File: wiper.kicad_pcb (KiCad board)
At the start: 2 copper layers, 90 x 67.5 mm, 68 parts, among them J1 Conn_01x02, J10 Conn_01x02, J2 Sensor FW, J3 Sensor BK, J4 Conn_01x02, J5 Conn_01x02, J6 PROG, J7 I2C, J8 UART, J9 Conn_01x02, K1 G5LE-1, K2 G5LE-1, Q1 MMBT2222A, Q2 MMBT2222A, Q3 MMBT2222A, Q4 MMBT2222A, SW1 Reset, U1 LM7805_TO220, U2 PC817, U3 PC817, U4 KA78M05_TO252, U5 ATmega48-20A, Y1 16MHz

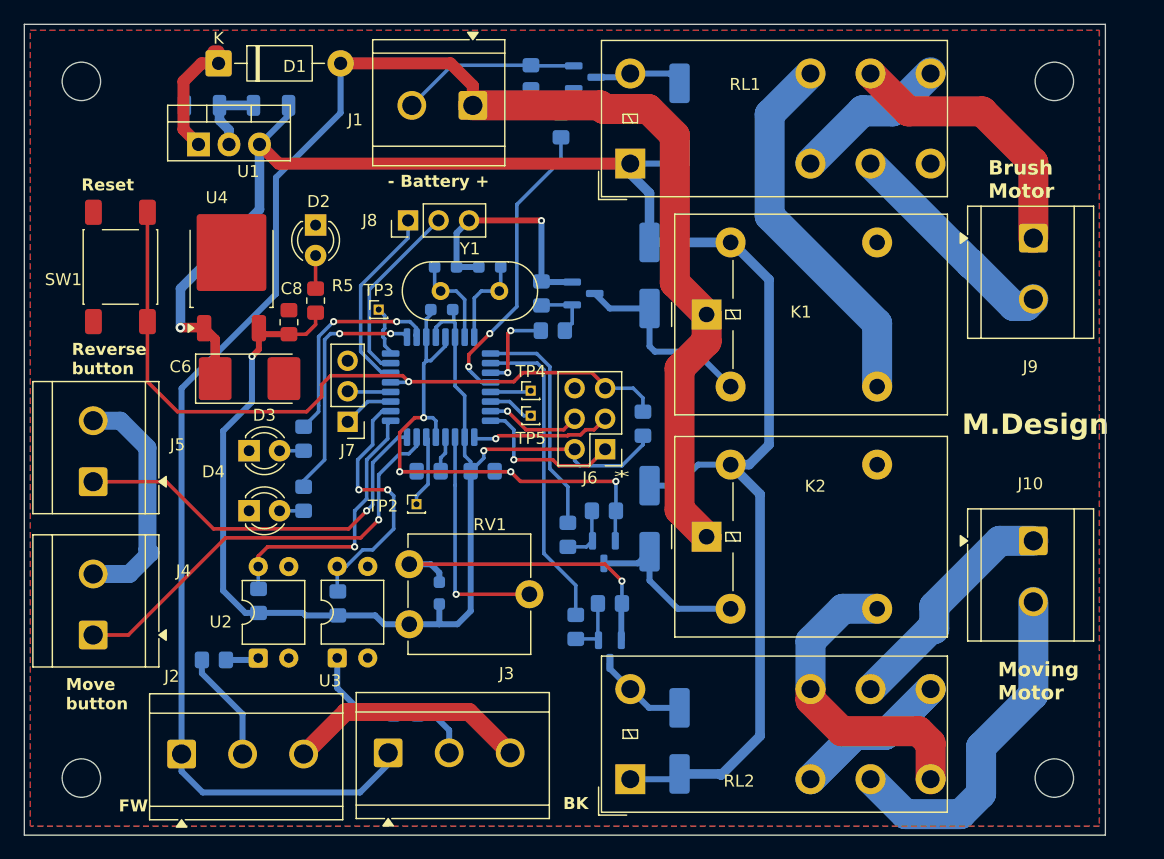
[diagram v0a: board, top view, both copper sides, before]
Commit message: New tracing finished. No mounting holes.
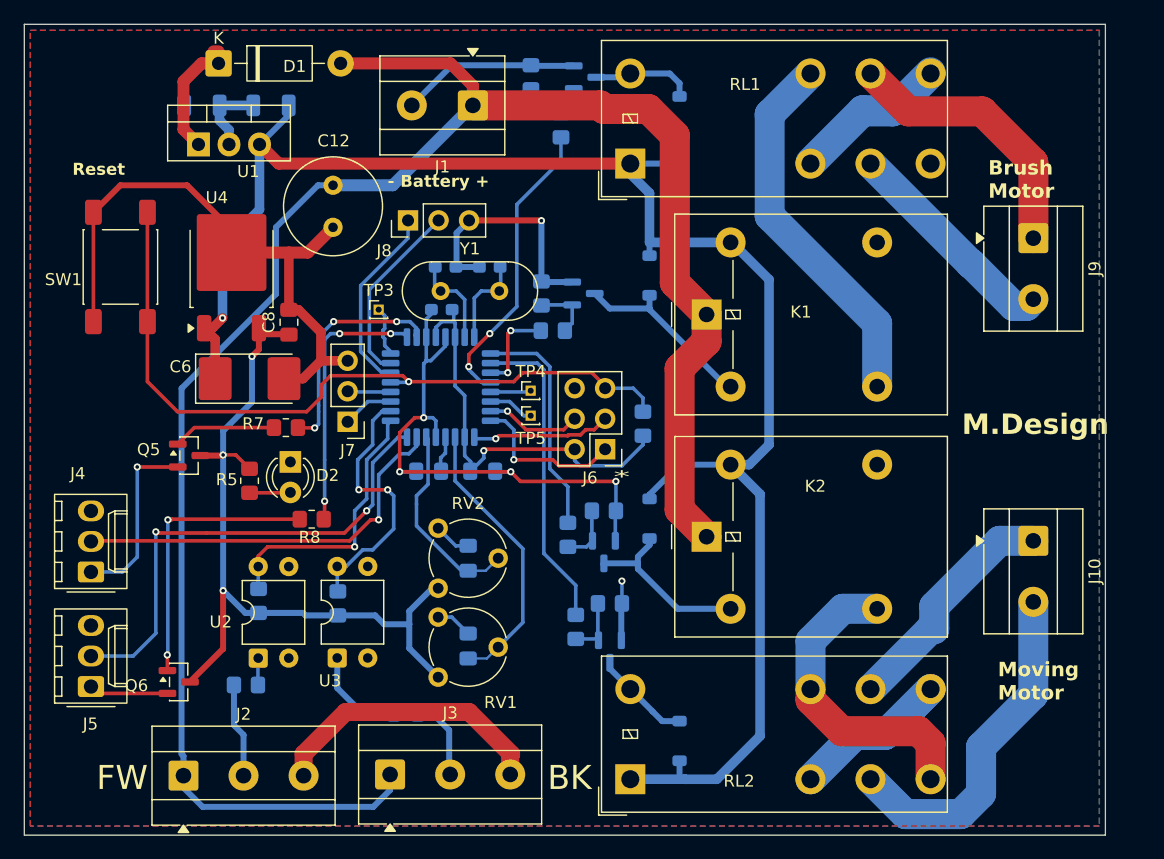
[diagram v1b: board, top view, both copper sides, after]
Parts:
- removed D3: LED MOVING, LED_THT:LED_D3.0mm
- removed D4: LED REVERSE, LED_THT:LED_D3.0mm
- removed REF** (x4): MountingHole_3.2mm_M3, MountingHole:MountingHole_3.2mm_M3
- removed TP2: ~, Connector_PinHeader_1.00mm:PinHeader_1x01_P1.00mm_Vertical
- added C11: 100nF, Capacitor_SMD:C_0805_2012Metric_Pad1.18x1.45mm_HandSolder, B.Cu at (175.2, 94.7)
- added C12: 47uFx100V, Capacitor_THT:C_Radial_D8.0mm_H7.0mm_P3.50mm, F.Cu at (163.9, 63.6)
- added Q5: MMBT2222A, Package_TO_SOT_SMD:SOT-23, F.Cu at (152.0, 86.2)
- added Q6: MMBT2222A, Package_TO_SOT_SMD:SOT-23, F.Cu at (151.1, 105.0)
- added RV2: 10K, Potentiometer_THT:Potentiometer_Piher_PT-6-V_Vertical, F.Cu at (172.7, 97.2)
- C1, C2: footprint Resistor_SMD:R_1206_3216Metric -> Capacitor_SMD:C_1206_3216Metric
- C10: footprint Resistor_SMD:R_0603_1608Metric_Pad0.98x0.95mm_HandSolder -> Capacitor_SMD:C_0805_2012Metric_Pad1.18x1.45mm_HandSolder
- C3, C4, C9: footprint Resistor_SMD:R_0603_1608Metric_Pad0.98x0.95mm_HandSolder -> Capacitor_SMD:C_0603_1608Metric_Pad1.08x0.95mm_HandSolder
- C5, C8: footprint Resistor_SMD:R_0805_2012Metric_Pad1.20x1.40mm_HandSolder -> Capacitor_SMD:C_0805_2012Metric_Pad1.18x1.45mm_HandSolder
- C7: value 100nF -> 10uF; footprint Resistor_SMD:R_0805_2012Metric_Pad1.20x1.40mm_HandSolder -> Capacitor_SMD:C_0805_2012Metric_Pad1.18x1.45mm_HandSolder
- D5, D6, D7, D8: value 1N4148 -> 1N4148W; footprint Diode_SMD:D_MiniMELF_Handsoldering -> Diode_SMD:D_SOD-123
- J1: value Conn_01x02 -> PWR_IN; footprint TerminalBlock_CUI:TerminalBlock_CUI_TB007-508-02_1x02_P5.08mm_Horizontal -> TerminalBlock_MetzConnect:TerminalBlock_MetzConnect_Type101_RT01602HBWC_1x02_P5.08mm_Horizontal
- J10: value Conn_01x02 -> MOTOR_MOVING; footprint TerminalBlock_CUI:TerminalBlock_CUI_TB007-508-02_1x02_P5.08mm_Horizontal -> TerminalBlock_MetzConnect:TerminalBlock_MetzConnect_Type101_RT01602HBWC_1x02_P5.08mm_Horizontal
- J2, J3: footprint TerminalBlock_CUI:TerminalBlock_CUI_TB007-508-03_1x03_P5.08mm_Horizontal -> TerminalBlock_MetzConnect:TerminalBlock_MetzConnect_Type055_RT01503HDWU_1x03_P5.00mm_Horizontal
- J4: value Conn_01x02 -> MOVE_BTN; footprint TerminalBlock_CUI:TerminalBlock_CUI_TB007-508-02_1x02_P5.08mm_Horizontal -> Connector_Molex:Molex_KK-254_AE-6410-03A_1x03_P2.54mm_Vertical
- J5: value Conn_01x02 -> REV_BTN; footprint TerminalBlock_CUI:TerminalBlock_CUI_TB007-508-02_1x02_P5.08mm_Horizontal -> Connector_Molex:Molex_KK-254_AE-6410-03A_1x03_P2.54mm_Vertical
- J9: value Conn_01x02 -> MOTOR_BRUSH; footprint TerminalBlock_CUI:TerminalBlock_CUI_TB007-508-02_1x02_P5.08mm_Horizontal -> TerminalBlock_MetzConnect:TerminalBlock_MetzConnect_Type101_RT01602HBWC_1x02_P5.08mm_Horizontal
- R7, R8: moved to F.Cu
- RV1: footprint Potentiometer_THT:Potentiometer_ACP_CA9-V10_Vertical -> Potentiometer_THT:Potentiometer_Piher_PT-6-V_Vertical
- U1: value LM7805_TO220 -> LM7812_TO220
- moved D2 19.8 mm to (160.4, 86.7)
- moved J5 17.1 mm to (143.8, 105.4)
- moved R5 16.0 mm to (157.0, 88.2), turned to -90 degrees
- moved J4 5.25 mm to (143.8, 95.8)
- moved C10 5.02 mm to (175.2, 102.0)
- moved RV1 5.02 mm to (172.7, 104.6)
- moved R1 3.39 mm to (156.7, 105.2)
- moved R8 1.83 mm to (162.2, 91.5), turned to 180 degrees
- moved J2 1.81 mm to (151.5, 112.8)
- moved J3 1.81 mm to (168.7, 112.7)
- moved R7 1.74 mm to (160.0, 83.8), turned to 180 degrees
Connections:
- C1 pad 2: Net-(U1-GND) -> ~
- C10 pad 1: +5V -> Net-(U5-ADC6)
- C2 pad 2: Net-(U1-GND) -> ~
- J4 pad 1: /MOVE_BTN -> Net-(J4-Pin_1)
- J4 pad 2: ~ -> /MOVE_BTN
- J5 pad 1: /REV_BTN -> Net-(J5-Pin_1)
- J5 pad 2: ~ -> /REV_BTN
- U1 pad 2: Net-(U1-GND) -> ~
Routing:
- net ~: track 200.3 -> 225.9 mm
- net Net-(Q6-B): track 2.00 -> 23.6 mm, vias 0 -> 2
- net Net-(J4-Pin_1): track 0.00 -> 15.2 mm, vias 0 -> 1
- net Net-(U5-ADC7): track 6.04 -> 16.6 mm
- net /REV_BTN: track 33.0 -> 40.9 mm, vias 1 -> 2
- net Net-(J5-Pin_1): track 0.00 -> 6.60 mm
- net Net-(Q5-B): track 2.00 -> 8.57 mm
- net Net-(U1-GND): track 6.40 -> 0.00 mm
- net +24V: track 206.1 -> 212.2 mm
- net Net-(U5-ADC6): track 19.2 -> 23.6 mm, vias 1 -> 0
- net /MOVE_BTN: track 36.4 -> 33.3 mm
- net +12V: track 144.7 -> 146.8 mm
- net Net-(U5-PD3): track 20.2 -> 22.2 mm, vias 2 -> 3
- net Net-(J3-Pin_2): track 5.09 -> 6.92 mm
- net Net-(J2-Pin_2): track 9.24 -> 7.88 mm
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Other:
- board text added: "Wiper ver. 3.0 15.10.2026"
- board text removed: "Move button"
- board text removed: "Reverse button"
- board text removed: "Wiper ver. 2.2 05.02.2026"
